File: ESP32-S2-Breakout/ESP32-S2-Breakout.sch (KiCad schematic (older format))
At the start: 37 parts, among them J1 USB_B_Micro, J2 Conn_01x21, J3 Conn_01x21, SW1 Reset, SW2 Boot, U1 USBLC6-2SC6, U2 ESP32-S2-WROOM, U3 XC6220B331MR, Y1 32.768KHz

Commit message: Add resistor values for 1.8V/2mA LEDs
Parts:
- R5: value TBD -> 750r
- R9: value TBD -> 1.6k
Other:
- note added: "Assume LED\n 1.8V 2mA"
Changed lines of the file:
@@
 AR Path="/5E6BFAB5/5E8A4E5B" Ref="R?"  Part="1"
 F 0 "R5" V 3254 6450 50  0000 C CNN
-F 1 "TBD" V 3345 6450 50  0000 C CNN
+F 1 "750r" V 3345 6450 50  0000 C CNN
 F 2 "Resistor_SMD:R_0603_1608Metric" H 3450 6450 50  0001 C CNN
 F 3 "~" H 3450 6450 50  0001 C CNN
@@
 P 6655 1750
 F 0 "R9" H 6714 1796 50  0000 L CNN
-F 1 "TBD" H 6714 1705 50  0000 L CNN
+F 1 "1.6k" H 6714 1705 50  0000 L CNN
 F 2 "Resistor_SMD:R_0603_1608Metric" H 6655 1750 50  0001 C CNN
 F 3 "~" H 6655 1750 50  0001 C CNN
@@
 Text Notes 5800 6800 0    100  ~ 0
 Mount Holes
+Text Notes 3750 6050 0    50   ~ 0
+Assume LED\n 1.8V 2mA
+Text Notes 6000 1950 0    50   ~ 0
+Assume LED\n 1.8V 2mA
 $EndSCHEMATC

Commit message: Add USB series termination resistor and bypass capacitor values
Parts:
- C10, C9: value TBD -> 20p
- R6, R7: value TBD -> 22r
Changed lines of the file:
@@
 AR Path="/5E6BFAB5/5E7FC958" Ref="R?"  Part="1"
 F 0 "R6" V 3804 6750 50  0000 C CNN
-F 1 "TBD" V 3895 6750 50  0000 C CNN
+F 1 "22r" V 3895 6750 50  0000 C CNN
 F 2 "Resistor_SMD:R_0603_1608Metric" H 4000 6750 50  0001 C CNN
 F 3 "~" H 4000 6750 50  0001 C CNN
@@
 AR Path="/5E6BFAB5/5E7FC95E" Ref="R?"  Part="1"
 F 0 "R7" V 4200 6900 50  0000 C CNN
-F 1 "TBD" V 4100 6900 50  0000 C CNN
+F 1 "22r" V 4100 6900 50  0000 C CNN
 F 2 "Resistor_SMD:R_0603_1608Metric" H 4000 6900 50  0001 C CNN
 F 3 "~" H 4000 6900 50  0001 C CNN
@@
 P 4450 6550
 F 0 "C9" H 4542 6596 50  0000 L CNN
-F 1 "TBD" H 4542 6505 50  0000 L CNN
+F 1 "20p" H 4542 6505 50  0000 L CNN
 F 2 "Capacitor_SMD:C_0603_1608Metric" H 4450 6550 50  0001 C CNN
 F 3 "~" H 4450 6550 50  0001 C CNN
@@
 P 4450 7100
 F 0 "C10" H 4542 7146 50  0000 L CNN
-F 1 "TBD" H 4542 7055 50  0000 L CNN
+F 1 "20p" H 4542 7055 50  0000 L CNN
 F 2 "Capacitor_SMD:C_0603_1608Metric" H 4450 7100 50  0001 C CNN
 F 3 "~" H 4450 7100 50  0001 C CNN

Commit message: Add resistor and capacitor values for 32.758kHz crystal
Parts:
- CL1, CL2: value TBD -> 11p C0G
- R1: value TBD -> N/C
- R2, R3: value TBD -> 220r 1%
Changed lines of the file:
@@
 	2300 3950 2100 3950
-$Comp
-L power:+3V3 #PWR02
-U 1 1 5E7FC8A3
-P 900 3950
-AR Path="/5E7FC8A3" Ref="#PWR02"  Part="1"
-AR Path="/5E6BFAB5/5E7FC8A3" Ref="#PWR?"  Part="1"
-F 0 "#PWR02" H 900 3800 50  0001 C CNN
-F 1 "+3V3" H 915 4123 50  0000 C CNN
-F 2 "" H 900 3950 50  0001 C CNN
-F 3 "" H 900 3950 50  0001 C CNN
-	1    900  3950
-	1    0    0    -1
-$EndComp
-$Comp
-L Device:C_Small C2
-U 1 1 5E7FC8A9
-P 900 4250
-AR Path="/5E7FC8A9" Ref="C2"  Part="1"
-AR Path="/5E6BFAB5/5E7FC8A9" Ref="C?"  Part="1"
-F 0 "C2" H 992 4296 50  0000 L CNN
-F 1 "22u" H 992 4205 50  0000 L CNN
-F 2 "Capacitor_SMD:C_0805_2012Metric" H 900 4250 50  0001 C CNN
-F 3 "~" H 900 4250 50  0001 C CNN
-	1    900  4250
-	1    0    0    -1
-$EndComp
-$Comp
-L Device:C_Small C3
-U 1 1 5E7FC8AF
-P 1250 4250
-AR Path="/5E7FC8AF" Ref="C3"  Part="1"
-AR Path="/5E6BFAB5/5E7FC8AF" Ref="C?"  Part="1"
-F 0 "C3" H 1342 4296 50  0000 L CNN
-F 1 "0.1u" H 1342 4205 50  0000 L CNN
-F 2 "Capacitor_SMD:C_0603_1608Metric" H 1250 4250 50  0001 C CNN
-F 3 "~" H 1250 4250 50  0001 C CNN
-	1    1250 4250
-	1    0    0    -1
-$EndComp
-$Comp
-L power:GND #PWR07
-U 1 1 5E7FC8B5
-P 1250 4450
-AR Path="/5E7FC8B5" Ref="#PWR07"  Part="1"
-AR Path="/5E6BFAB5/5E7FC8B5" Ref="#PWR?"  Part="1"
-F 0 "#PWR07" H 1250 4200 50  0001 C CNN
-F 1 "GND" H 1255 4277 50  0000 C CNN
-F 2 "" H 1250 4450 50  0001 C CNN
-F 3 "" H 1250 4450 50  0001 C CNN
-	1    1250 4450
-	-1   0    0    -1
-$EndComp
-Wire Wire Line
-	900  4050 1250 4050
-Wire Wire Line
-	1250 4450 1250 4350
-Wire Wire Line
-	1250 4150 1250 4050
-Connection ~ 1250 4050
-Wire Wire Line
-	900  4150 900  4050
-Connection ~ 900  4050
-Wire Wire Line
-	900  4050 900  3950
-$Comp
-L power:GND #PWR03
-U 1 1 5E7FC8C3
-P 900 4450
-AR Path="/5E7FC8C3" Ref="#PWR03"  Part="1"
-AR Path="/5E6BFAB5/5E7FC8C3" Ref="#PWR?"  Part="1"
-F 0 "#PWR03" H 900 4200 50  0001 C CNN
-F 1 "GND" H 905 4277 50  0000 C CNN
-F 2 "" H 900 4450 50  0001 C CNN
-F 3 "" H 900 4450 50  0001 C CNN
-	1    900  4450
-	-1   0    0    -1
-$EndComp
-Wire Wire Line
-	900  4450 900  4350
 $Comp
 L Device:C_Small C4
@@
 AR Path="/5E6BFAB5/5E7FC96C" Ref="CL?"  Part="1"
 F 0 "CL1" V 1121 6400 50  0000 C CNN
-F 1 "TBD" V 1212 6400 50  0000 C CNN
+F 1 "11p C0G" V 1212 6400 50  0000 C CNN
 F 2 "Capacitor_SMD:C_0603_1608Metric" H 1350 6400 50  0001 C CNN
 F 3 "~" H 1350 6400 50  0001 C CNN
@@
 AR Path="/5E6BFAB5/5E7FC972" Ref="CL?"  Part="1"
 F 0 "CL2" V 1550 6600 50  0000 C CNN
-F 1 "TBD" V 1450 6600 50  0000 C CNN
+F 1 "11p C0G" V 1450 6600 50  0000 C CNN
 F 2 "Capacitor_SMD:C_0603_1608Metric" H 1350 6600 50  0001 C CNN
 F 3 "~" H 1350 6600 50  0001 C CNN
@@
 AR Path="/5E6BFAB5/5E7FC98E" Ref="R?"  Part="1"
 F 0 "R1" H 2091 6454 50  0000 R CNN
-F 1 "TBD" H 2091 6545 50  0000 R CNN
+F 1 "N/C" H 2091 6545 50  0000 R CNN
 F 2 "Resistor_SMD:R_0603_1608Metric" H 2150 6500 50  0001 C CNN
 F 3 "~" H 2150 6500 50  0001 C CNN
@@
 AR Path="/5E6BFAB5/5E7FC994" Ref="R?"  Part="1"
 F 0 "R2" V 2746 6400 50  0000 C CNN
-F 1 "TBD" V 2655 6400 50  0000 C CNN
+F 1 "220r 1%" V 2655 6400 50  0000 C CNN
 F 2 "Resistor_SMD:R_0603_1608Metric" H 2550 6400 50  0001 C CNN
 F 3 "~" H 2550 6400 50  0001 C CNN
@@
 AR Path="/5E6BFAB5/5E7FC99A" Ref="R?"  Part="1"
 F 0 "R3" V 2750 6600 50  0000 C CNN
-F 1 "TBD" V 2650 6600 50  0000 C CNN
+F 1 "220r 1%" V 2650 6600 50  0000 C CNN
 F 2 "Resistor_SMD:R_0603_1608Metric" H 2550 6600 50  0001 C CNN
 F 3 "~" H 2550 6600 50  0001 C CNN
@@
 	6950 5565 6950 5665
 Connection ~ 6950 5565
-Wire Wire Line
-	1250 4050 2300 4050
 Text Label 4850 6750 0    50   ~ 0
 USB_D+
@@
 Text Notes 6000 1950 0    50   ~ 0
 Assume LED\n 1.8V 2mA
+$Comp
+L Device:C_Small C3
+U 1 1 5E7FC8AF
+P 1250 4250
+AR Path="/5E7FC8AF" Ref="C3"  Part="1"
+AR Path="/5E6BFAB5/5E7FC8AF" Ref="C?"  Part="1"
+F 0 "C3" H 1342 4296 50  0000 L CNN
+F 1 "0.1u" H 1342 4205 50  0000 L CNN
+F 2 "Capacitor_SMD:C_0603_1608Metric" H 1250 4250 50  0001 C CNN
+F 3 "~" H 1250 4250 50  0001 C CNN
+	1    1250 4250
+	1    0    0    -1
+$EndComp
+$Comp
+L power:GND #PWR07
+U 1 1 5E7FC8B5
+P 1250 4450
+AR Path="/5E7FC8B5" Ref="#PWR07"  Part="1"
+AR Path="/5E6BFAB5/5E7FC8B5" Ref="#PWR?"  Part="1"
+F 0 "#PWR07" H 1250 4200 50  0001 C CNN
+F 1 "GND" H 1255 4277 50  0000 C CNN
+F 2 "" H 1250 4450 50  0001 C CNN
+F 3 "" H 1250 4450 50  0001 C CNN
+	1    1250 4450
+	-1   0    0    -1
+$EndComp
+Wire Wire Line
+	1250 4450 1250 4350
+Wire Wire Line
+	1250 4150 1250 4050
+Wire Wire Line
+	900  4050 1250 4050
+Wire Wire Line
+	900  4450 900  4350
+$Comp
+L power:GND #PWR03
+U 1 1 5E7FC8C3
+P 900 4450
+AR Path="/5E7FC8C3" Ref="#PWR03"  Part="1"
+AR Path="/5E6BFAB5/5E7FC8C3" Ref="#PWR?"  Part="1"
+F 0 "#PWR03" H 900 4200 50  0001 C CNN
+F 1 "GND" H 905 4277 50  0000 C CNN
+F 2 "" H 900 4450 50  0001 C CNN
+F 3 "" H 900 4450 50  0001 C CNN
+	1    900  4450
+	-1   0    0    -1
+$EndComp
+Wire Wire Line
+	900  4050 900  3950
+Connection ~ 900  4050
+Wire Wire Line
+	900  4150 900  4050
+$Comp
+L Device:C_Small C2
+U 1 1 5E7FC8A9
+P 900 4250
+AR Path="/5E7FC8A9" Ref="C2"  Part="1"
+AR Path="/5E6BFAB5/5E7FC8A9" Ref="C?"  Part="1"
+F 0 "C2" H 992 4296 50  0000 L CNN
+F 1 "22u" H 992 4205 50  0000 L CNN
+F 2 "Capacitor_SMD:C_0805_2012Metric" H 900 4250 50  0001 C CNN
+F 3 "~" H 900 4250 50  0001 C CNN
+	1    900  4250
+	1    0    0    -1
+$EndComp
+$Comp
+L power:+3V3 #PWR02
+U 1 1 5E7FC8A3
+P 900 3950
+AR Path="/5E7FC8A3" Ref="#PWR02"  Part="1"
+AR Path="/5E6BFAB5/5E7FC8A3" Ref="#PWR?"  Part="1"
+F 0 "#PWR02" H 900 3800 50  0001 C CNN
+F 1 "+3V3" H 915 4123 50  0000 C CNN
+F 2 "" H 900 3950 50  0001 C CNN
+F 3 "" H 900 3950 50  0001 C CNN
+	1    900  3950
+	1    0    0    -1
+$EndComp
+Connection ~ 1250 4050
+Wire Wire Line
+	1250 4050 2300 4050
 $EndSCHEMATC

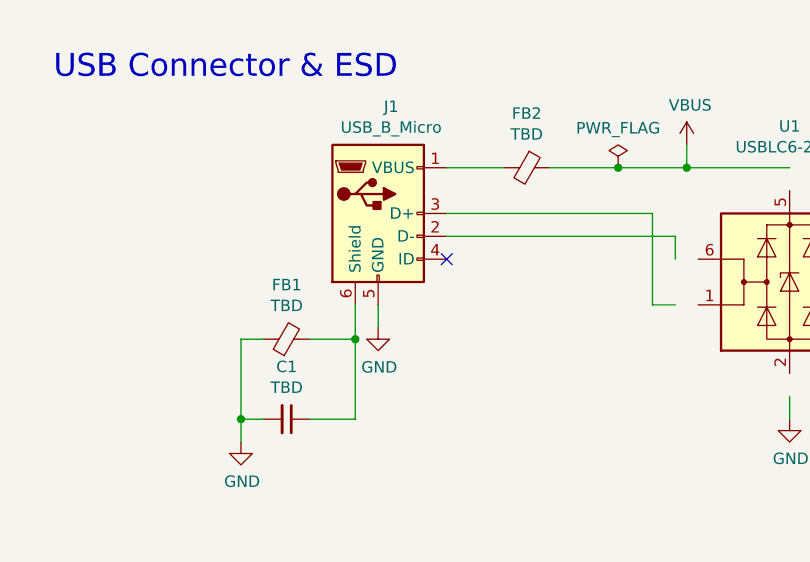
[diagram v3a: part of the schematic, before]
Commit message: Add values for ferrite bead on usb connector
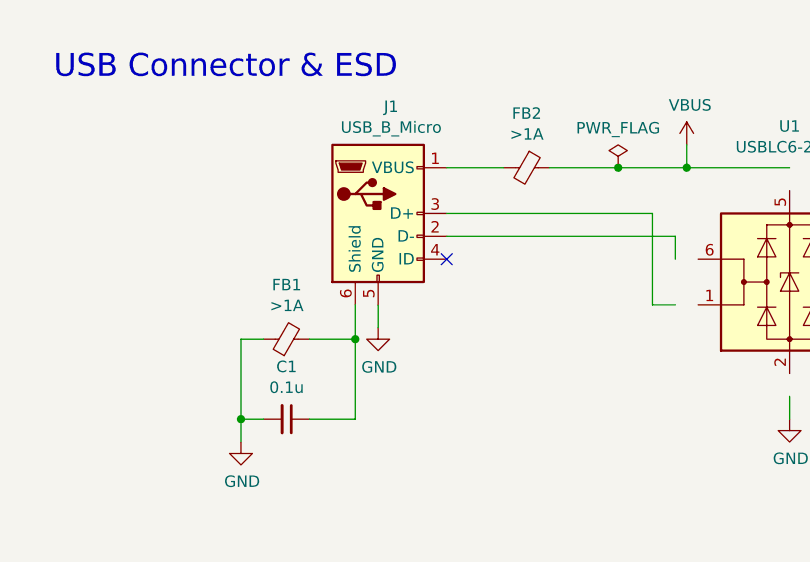
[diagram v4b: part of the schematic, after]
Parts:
- C1: value TBD -> 0.1u
- FB1, FB2: value TBD -> >1A
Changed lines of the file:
@@
 AR Path="/5E7E0058" Ref="FB2"  Part="1"
 F 0 "FB2" V 2483 1130 50  0000 C CNN
-F 1 "TBD" V 2574 1130 50  0000 C CNN
+F 1 ">1A" V 2574 1130 50  0000 C CNN
 F 2 "Inductor_SMD:L_0603_1608Metric" V 2650 1130 50  0001 C CNN
 F 3 "~" H 2720 1130 50  0001 C CNN
@@
 P 1670 1880
 F 0 "FB1" V 1907 1880 50  0000 C CNN
-F 1 "TBD" V 1816 1880 50  0000 C CNN
+F 1 ">1A" V 1816 1880 50  0000 C CNN
 F 2 "Inductor_SMD:L_0603_1608Metric" V 1600 1880 50  0001 C CNN
 F 3 "~" H 1670 1880 50  0001 C CNN
@@
 P 1670 2230
 F 0 "C1" V 1441 2230 50  0000 C CNN
-F 1 "TBD" V 1532 2230 50  0000 C CNN
+F 1 "0.1u" V 1532 2230 50  0000 C CNN
 F 2 "Capacitor_SMD:C_0603_1608Metric" H 1670 2230 50  0001 C CNN
 F 3 "~" H 1670 2230 50  0001 C CNN

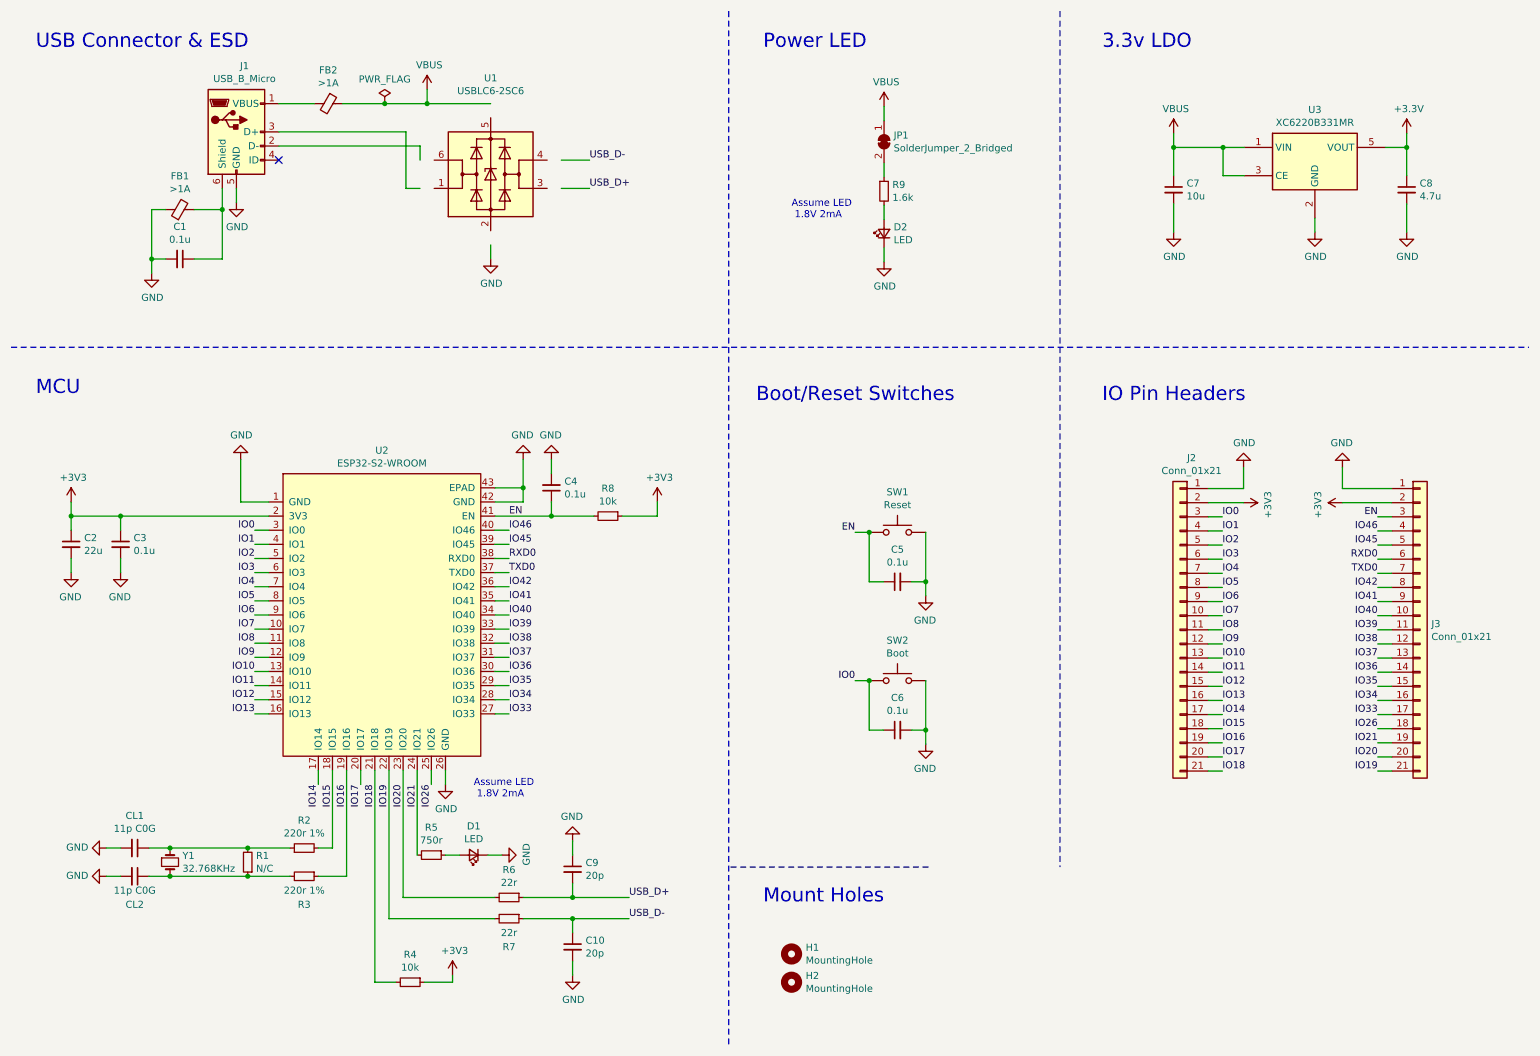
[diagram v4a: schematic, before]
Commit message: Add 5v and extra gnd pin to pin headers, rearrange pcb
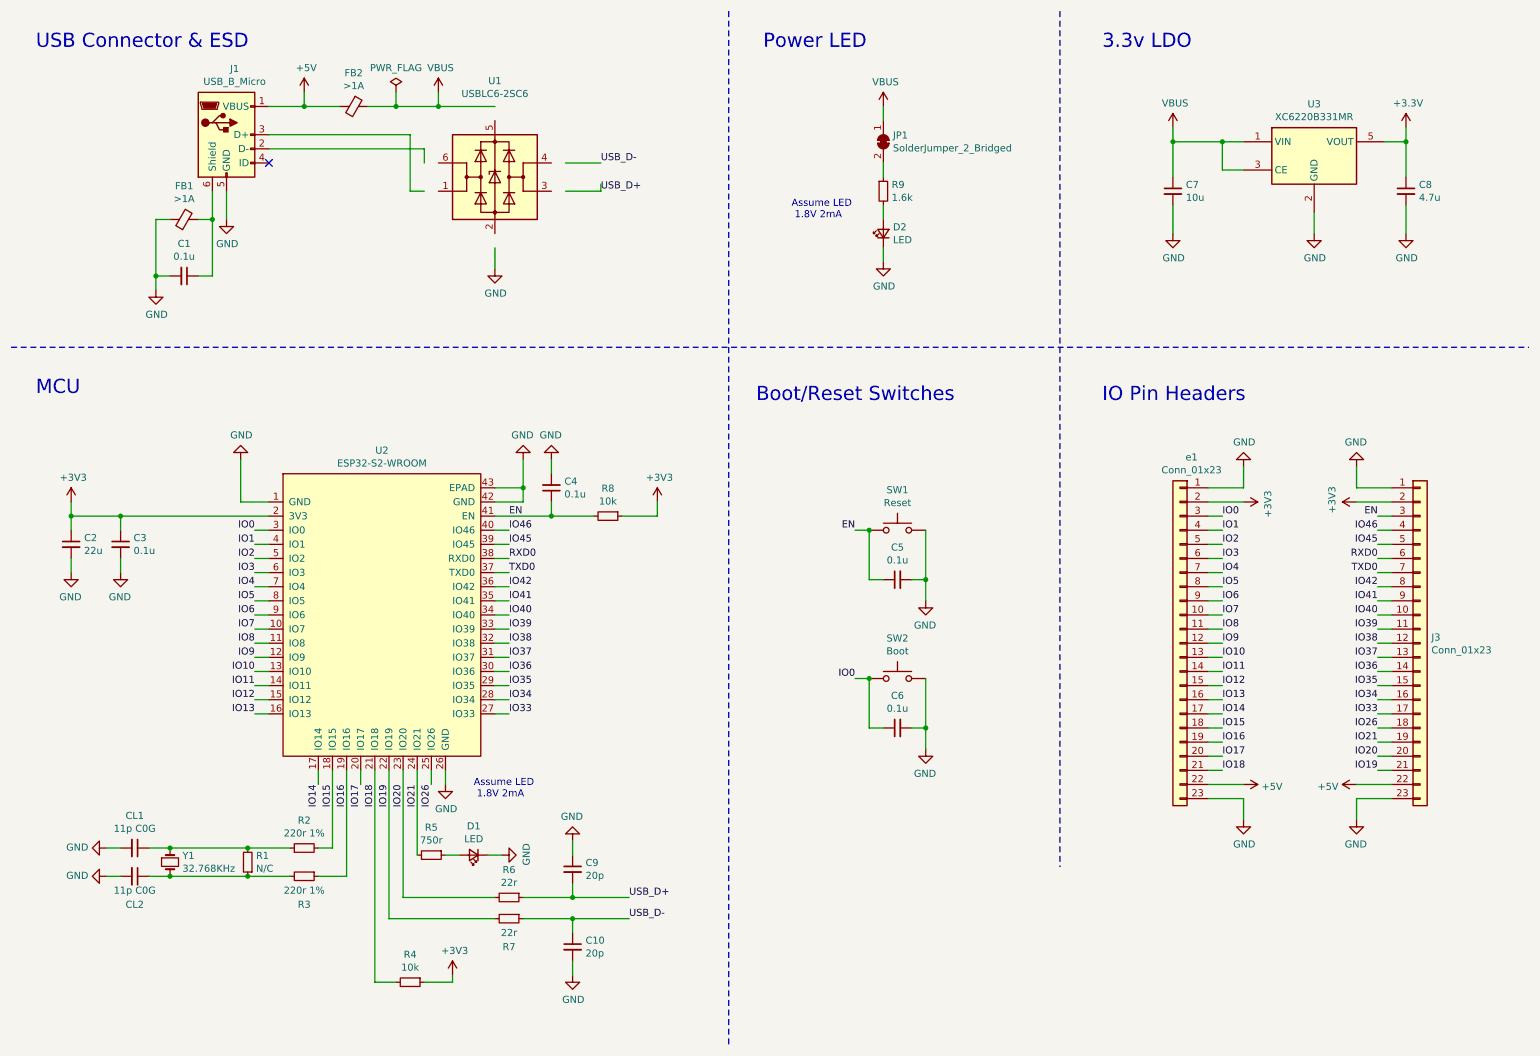
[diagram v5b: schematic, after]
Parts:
- removed H1, H2: MountingHole, MountingHole:MountingHole_2.2mm_M2_Pad_Via, symbol Mechanical:MountingHole
- removed J2, J3: Conn_01x21, Connector_PinHeader_2.54mm:PinHeader_1x21_P2.54mm_Vertical, symbol Connector_Generic:Conn_01x21
- added J3, e1: Conn_01x23, Connector_PinHeader_2.54mm:PinHeader_1x23_P2.54mm_Vertical, symbol Connector_Generic:Conn_01x23
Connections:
- net labels added: +5V
- wire segments 176 -> 186
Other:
- note removed: "Mount Holes"
- moved on the sheet: C1, FB1, FB2, J1, U1, U3

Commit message: Change all passives from 0603 to 0805 Add capacitor to input pin of USBLC6 Update gerbers and images
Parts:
- added C11: 0.1u, Capacitor_SMD:C_0805_2012Metric, symbol Device:C_Small
- C1, C10, C3, C4, C5, C6, C7, C8, C9, CL1, CL2: footprint Capacitor_SMD:C_0603_1608Metric -> Capacitor_SMD:C_0805_2012Metric
- D1, D2: footprint LED_SMD:LED_0603_1608Metric -> LED_SMD:LED_0805_2012Metric
- FB1, FB2: footprint Inductor_SMD:L_0603_1608Metric -> Inductor_SMD:L_0805_2012Metric
- R1, R2, R3, R4, R5, R6, R7, R8, R9: footprint Resistor_SMD:R_0603_1608Metric -> Resistor_SMD:R_0805_2012Metric
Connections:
- wire segments 186 -> 187
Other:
- moved on the sheet: FB2, U1

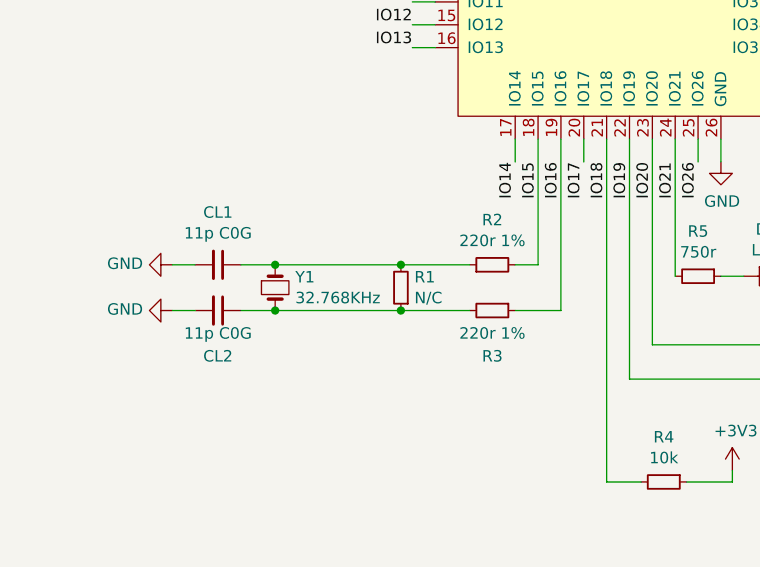
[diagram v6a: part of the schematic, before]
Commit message: Update crystal passive values and readme
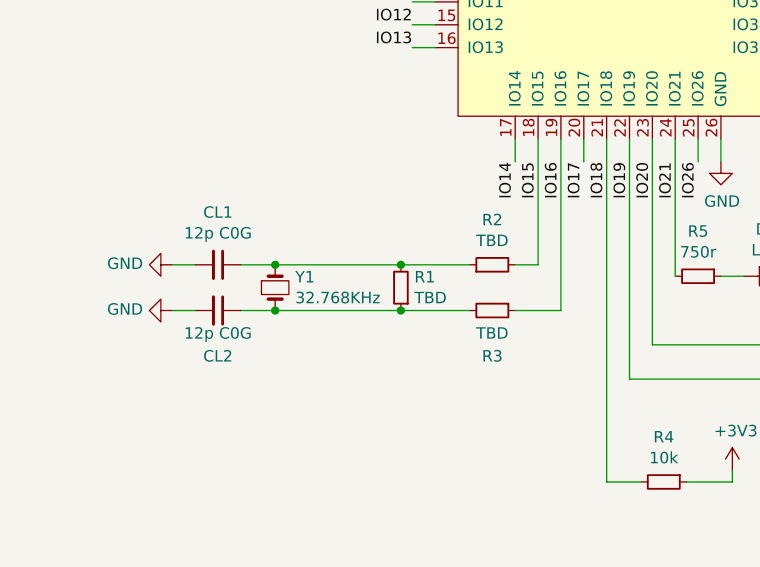
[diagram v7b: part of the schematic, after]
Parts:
- CL1, CL2: value 11p C0G -> 12p C0G
- R1: value N/C -> TBD
- R2, R3: value 220r 1% -> TBD
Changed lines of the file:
@@
 AR Path="/5E6BFAB5/5E7FC96C" Ref="CL?"  Part="1"
 F 0 "CL1" V 1121 6400 50  0000 C CNN
-F 1 "11p C0G" V 1212 6400 50  0000 C CNN
+F 1 "12p C0G" V 1212 6400 50  0000 C CNN
 F 2 "Capacitor_SMD:C_0805_2012Metric" H 1350 6400 50  0001 C CNN
 F 3 "~" H 1350 6400 50  0001 C CNN
@@
 AR Path="/5E6BFAB5/5E7FC972" Ref="CL?"  Part="1"
 F 0 "CL2" V 1550 6600 50  0000 C CNN
-F 1 "11p C0G" V 1450 6600 50  0000 C CNN
+F 1 "12p C0G" V 1450 6600 50  0000 C CNN
 F 2 "Capacitor_SMD:C_0805_2012Metric" H 1350 6600 50  0001 C CNN
 F 3 "~" H 1350 6600 50  0001 C CNN
@@
 AR Path="/5E6BFAB5/5E7FC98E" Ref="R?"  Part="1"
 F 0 "R1" H 2091 6454 50  0000 R CNN
-F 1 "N/C" H 2091 6545 50  0000 R CNN
+F 1 "TBD" H 2091 6545 50  0000 R CNN
 F 2 "Resistor_SMD:R_0805_2012Metric" H 2150 6500 50  0001 C CNN
 F 3 "~" H 2150 6500 50  0001 C CNN
@@
 AR Path="/5E6BFAB5/5E7FC994" Ref="R?"  Part="1"
 F 0 "R2" V 2746 6400 50  0000 C CNN
-F 1 "220r 1%" V 2655 6400 50  0000 C CNN
+F 1 "TBD" V 2655 6400 50  0000 C CNN
 F 2 "Resistor_SMD:R_0805_2012Metric" H 2550 6400 50  0001 C CNN
 F 3 "~" H 2550 6400 50  0001 C CNN
@@
 AR Path="/5E6BFAB5/5E7FC99A" Ref="R?"  Part="1"
 F 0 "R3" V 2750 6600 50  0000 C CNN
-F 1 "220r 1%" V 2650 6600 50  0000 C CNN
+F 1 "TBD" V 2650 6600 50  0000 C CNN
 F 2 "Resistor_SMD:R_0805_2012Metric" H 2550 6600 50  0001 C CNN
 F 3 "~" H 2550 6600 50  0001 C CNN
